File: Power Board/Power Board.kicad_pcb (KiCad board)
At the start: 2 copper layers, 80 x 45.7 mm, 61 parts, among them J1 Conn_02x15_Counter_Clockwise, Q1 SI7135DP, Q2 SI7135DP, Q3 SI7135DP, Q4 SI7135DP, Q5 SI7135DP, Q6 SI7135DP, U1 LTC4417CGN, U2 TPS54308DDC, U3 TPS54308DDC, U4 LTC3130-1

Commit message: Last commit before I change the board shape
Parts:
- moved C23 2.06 mm to (93.3, 116.2), turned to 270 degrees
- moved C20 1.27 mm to (96.0, 112.3)
- moved C22 1.27 mm to (95.5, 114.3)
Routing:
- net +3V3: track 79.0 -> 88.8 mm, vias 5 -> 9
- net /VCC_IN: track 114.2 -> 113.0 mm
- net Net-(C23-Pad1): track 2.15 -> 3.14 mm
- net GND: vias 87 -> 85
- removed copper zone on F.Cu, net +14V
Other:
- board text added: "Power Board v0.6 UAH SHC Spaceport America Cup 2018 Designed by Thomas Bennett & Daniel Corey"
- board text removed: "Power Board v0.5 UAH SHC Spaceport America Cup 2018 Designed by Thomas Bennett"

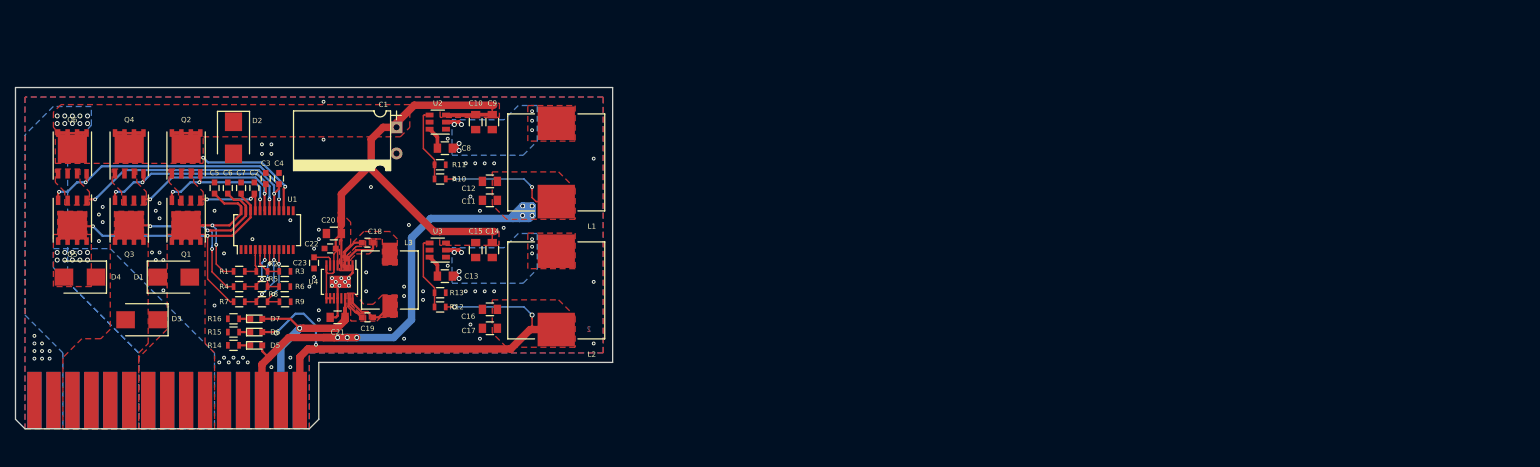
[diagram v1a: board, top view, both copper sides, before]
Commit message: New Board shape
Thanks a lot James
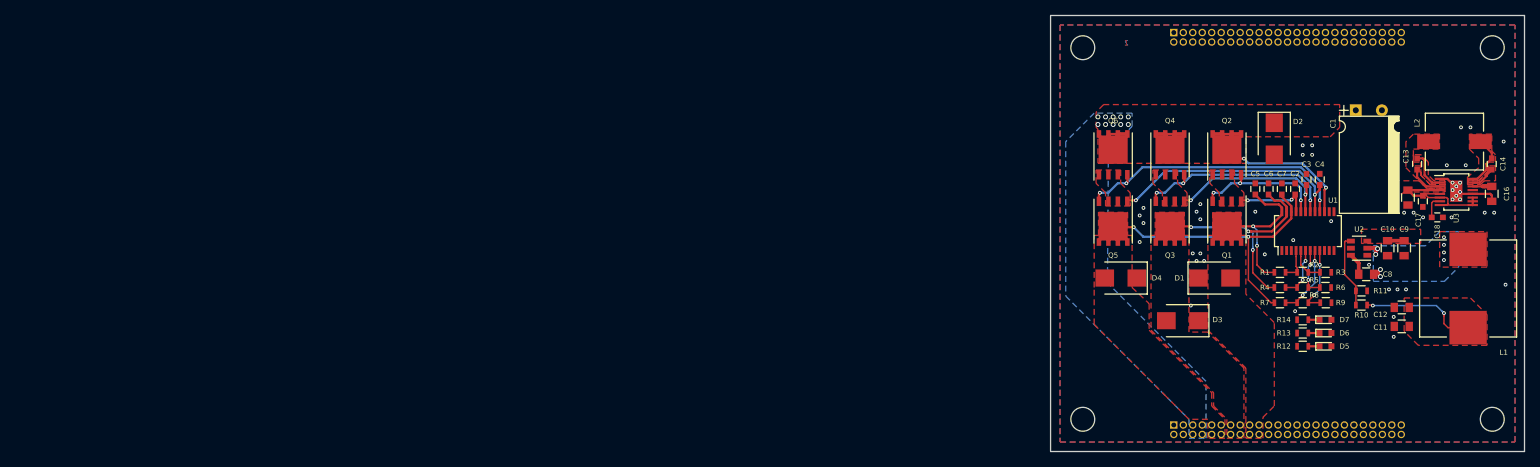
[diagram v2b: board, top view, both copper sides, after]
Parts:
- removed C19: 22nF, Capacitors_SMD:C_0603
- removed C20: 15 uF, Capacitors_SMD:C_0805
- removed C21: 22 uF, Capacitors_SMD:C_0805
- removed C22: 1 uF, Capacitors_SMD:C_0603
- removed C23: 4.7 uF, Capacitors_SMD:C_0603
- removed G***: LOGO, Custom Parts:Logo_v2
- removed L3: 15 uH, Custom Footprints:L_Wuerth_7447779115
- removed R15: 100 Ω, Resistors_SMD:R_0603
- removed R16: 470 Ω, Resistors_SMD:R_0603
- removed U4: LTC3130-1, Housings_SSOP:MSOP-16-1EP_3x4mm_Pitch0.5mm
- added H1: M3 Mounting Hole, Mounting_Holes:MountingHole_3.2mm_M3, F.Cu at (196.3, 87.4)
- added H2: M3 Mounting Hole, Mounting_Holes:MountingHole_3.2mm_M3, F.Cu at (251.2, 87.4)
- added H3: M3 Mounting Hole, Mounting_Holes:MountingHole_3.2mm_M3, F.Cu at (196.3, 137.2)
- added H4: M3 Mounting Hole, Mounting_Holes:MountingHole_3.2mm_M3, F.Cu at (251.2, 137.2)
- added J2: Conn_02x25_Odd_Even, Pin_Headers:Pin_Header_Straight_2x25_Pitch1.27mm, B.Cu at (208.5, 85.3)
- added SYM1: SYM_Arrow45_XLarge, Custom Parts:Logo_v3, B.Cu at (218.2, 121.9)
- C13: value 0.1 uF -> 22nF; footprint Capacitors_SMD:C_0805 -> Capacitors_SMD:C_0603
- C14: value 15 uF -> 22nF; footprint Capacitors_SMD:C_0805 -> Capacitors_SMD:C_0603
- C17: value 22 uF -> 1 uF; footprint Capacitors_SMD:C_0805 -> Capacitors_SMD:C_0603
- C18: value 22nF -> 4.7 uF
- J1: value Conn_02x15_Counter_Clockwise -> Conn_02x25_Odd_Even; footprint Custom Footprints:CONN_CARD_02x15_MALE -> Pin_Headers:Pin_Header_Straight_2x25_Pitch1.27mm; moved to B.Cu
- L2: value 18 uH -> 15 uH; footprint Inductors_SMD:L_Wuerth_HCI-1365 -> Custom Footprints:L_Wuerth_7447779115
- R12: value 100 kΩ -> 100 Ω
- R13: value 22 kΩ -> 100 Ω
- R14: value 100 Ω -> 470 Ω
- U3: value TPS54308DDC -> LTC3130-1; footprint TO_SOT_Packages_SMD:SOT-23-6 -> Housings_SSOP:MSOP-16-1EP_3x4mm_Pitch0.5mm
- moved C18 143.4 mm to (243.8, 110.1), turned to 0 degrees
- moved R14 143.3 mm to (225.8, 123.8)
- moved D5 143.3 mm to (228.9, 127.4)
- moved D6 143.3 mm to (228.9, 125.6)
- moved D7 143.3 mm to (228.9, 123.8)
- moved J1 141.2 mm to (208.5, 137.9), turned to 270 degrees
- moved C4 139.4 mm to (228.1, 105.0)
- moved C6 139.4 mm to (221.2, 106.3)
- moved D2 139.4 mm to (222.0, 99.6)
- moved D3 139.4 mm to (209.7, 124.0)
- moved D4 139.4 mm to (201.4, 118.2)
- moved Q3 139.4 mm to (208.0, 110.6)
- moved Q4 139.4 mm to (208.0, 101.7)
- moved R1 139.4 mm to (222.8, 117.5)
- moved R2 139.4 mm to (225.8, 117.5)
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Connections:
- C14 pad 1: /VCC_IN -> Net-(C14-Pad1)
- C14 pad 2: GND -> Net-(C14-Pad2)
- C16 pad 1: /XBEE_VCC -> +12V
- C17 pad 1: /XBEE_VCC -> /VCC_IN
- C18 pad 2: Net-(C18-Pad2) -> GND
- D6 pad 2: /XBEE_VCC -> +3V3
- J1 pad 10: /UMB_VCC -> /BAT_BAK_VCC
- J1 pad 11: GND -> /BAT_BAK_VCC
- J1 pad 12: GND -> /BAT_BAK_VCC
- J1 pad 13: +3V3 -> /BAT_VCC
- J1 pad 14: GND -> /BAT_VCC
- J1 pad 15: /XBEE_VCC -> /BAT_VCC
- J1 pad 16: GND -> /BAT_VCC
- J1 pad 17: +12V -> /UMB_VCC
- J1 pad 18: GND -> /UMB_VCC
- J1 pad 19: GND -> /UMB_VCC
- J1 pad 20: GND -> /UMB_VCC
- J1 pad 21: /BAT_BAK_VCC -> GND
- J1 pad 22: /BAT_BAK_VCC -> GND
- J1 pad 23: /BAT_BAK_VCC -> GND
- J1 pad 24: /BAT_BAK_VCC -> GND
- J1 pad 25: /VCC_IN -> (no net)
- J1 pad 26: /VCC_IN -> (no net)
- J1 pad 27: /VCC_IN -> (no net)
- J1 pad 28: /VCC_IN -> (no net)
- J1 pad 29: GND -> (no net)
- J1 pad 3: /BAT_VCC -> GND
- J1 pad 30: GND -> (no net)
- J1 pad 4: /BAT_VCC -> GND
- J1 pad 5: /BAT_VCC -> /VCC_IN
- J1 pad 6: /BAT_VCC -> /VCC_IN
- J1 pad 7: /UMB_VCC -> /VCC_IN
- J1 pad 8: /UMB_VCC -> /VCC_IN
- J1 pad 9: /UMB_VCC -> /BAT_BAK_VCC
- L2 pad 2: /XBEE_VCC -> Net-(C14-Pad1)
- R12 pad 1: /XBEE_VCC -> Net-(D5-Pad1)
- R12 pad 2: Net-(R12-Pad2) -> GND
- R13 pad 1: Net-(R12-Pad2) -> Net-(D6-Pad1)
- R14 pad 1: Net-(D5-Pad1) -> Net-(D7-Pad1)
- U3 pad 2: Net-(C13-Pad2) -> Net-(C13-Pad1)
- U3 pad 3: /VCC_IN -> Net-(C13-Pad2)
- U3 pad 4: Net-(R12-Pad2) -> /VCC_IN
- U3 pad 5: (no net) -> /VCC_IN
- U3 pad 6: Net-(C13-Pad1) -> /VCC_IN
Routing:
- net +3V3: track 88.8 -> 15.7 mm, vias 9 -> 2
- net /XBEE_VCC: track 70.9 -> 0.00 mm, vias 4 -> 0
- net /VCC_IN: track 113.0 -> 51.1 mm
- net +12V: track 26.9 -> 3.74 mm, vias 1 -> 0
- net Net-(R12-Pad2): track 9.96 -> 0.00 mm
- net Net-(C19-Pad1): track 7.04 -> 0.00 mm
- net Net-(C14-Pad1): track 0.00 -> 7.04 mm
- net Net-(C18-Pad2): track 4.58 -> 0.00 mm
- net Net-(C19-Pad2): track 3.36 -> 0.00 mm
- net Net-(C14-Pad2): track 0.00 -> 3.36 mm
- net Net-(C23-Pad1): track 3.14 -> 0.00 mm
- net Net-(C13-Pad1): track 2.98 -> 5.57 mm
- net Net-(C18-Pad1): track 5.57 -> 3.14 mm
- net Net-(C13-Pad2): track 5.67 -> 4.58 mm, vias 7 -> 0
- net Net-(C8-Pad2): track 5.67 -> 5.50 mm, vias 7 -> 8
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- removed copper zone on B.Cu, net /BAT_BAK_VCC
- removed copper zone on F.Cu, net /XBEE_VCC
- removed copper zone on B.Cu, net Net-(C13-Pad2)
- removed copper zone on F.Cu, net Net-(C13-Pad2)
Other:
- board size 80 x 45.7 mm -> 63.5 x 58.4 mm
- board text added: "Power Board v0.7 UAH SHC Spaceport America Cup 2018 Designed by Thomas Bennett & Daniel Corey"
- board text removed: "Power Board v0.6 UAH SHC Spaceport America Cup 2018 Designed by Thomas Bennett & Daniel Corey"

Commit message: A whole lot of changes
Kinda forgot what they all were
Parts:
- removed D1, D3, D4: SMBJ26CA, Diodes_SMD:D_SMB
- removed the D6 at (228.9, 125.6)
- removed the R13 at (225.8, 125.6)
- added J3: Conn_01x02, Custom Footprints:High_Current_Wires, F.Cu at (251.7, 117.6)
- added J4: Conn_01x02, Custom Footprints:High_Current_Wires, F.Cu at (251.7, 106.9)
- added J5: Conn_01x02, Custom Footprints:High_Current_Wires, F.Cu at (251.7, 96.0)
- J1: value Conn_02x25_Odd_Even -> Conn_02x10_Odd_Even; footprint Pin_Headers:Pin_Header_Straight_2x25_Pitch1.27mm -> Pin_Headers:Pin_Header_Straight_2x10_Pitch1.27mm
- J2: value Conn_02x25_Odd_Even -> Conn_01x02; footprint Pin_Headers:Pin_Header_Straight_2x25_Pitch1.27mm -> Custom Footprints:High_Current_Wires; moved to F.Cu
- moved J2 61.1 mm to (251.7, 128.5), turned to 90 degrees
- moved R12 40.9 mm to (200.7, 95.1), turned to 90 degrees
- moved D5 40.6 mm to (200.7, 98.2), turned to 270 degrees
- moved D6 39.6 mm to (198.6, 98.2), turned to 270 degrees
- moved R13 39.5 mm to (198.6, 95.1), turned to 90 degrees
- moved C13 35.3 mm to (207.6, 91.8)
- moved C14 35.3 mm to (217.6, 91.8)
- moved C15 35.3 mm to (206.4, 96.3)
- moved C16 35.3 mm to (217.6, 95.8)
- moved C17 35.3 mm to (208.4, 96.8)
- moved C18 35.3 mm to (210.3, 98.9)
- moved L2 35.3 mm to (212.6, 88.8)
- moved U3 35.3 mm to (212.9, 95.5)
- moved Q6 33.2 mm to (209.7, 133.6), turned to 180 degrees
- moved D2 33.2 mm to (201.9, 126.0)
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- renumbered D7 to D6, R14 to R13
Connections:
- J1 pad 1: GND -> +3V3
- J1 pad 11: /BAT_BAK_VCC -> (no net)
- J1 pad 12: /BAT_BAK_VCC -> GND
- J1 pad 13: /BAT_VCC -> (no net)
- J1 pad 14: /BAT_VCC -> +3V3
- J1 pad 15: /BAT_VCC -> (no net)
- J1 pad 16: /BAT_VCC -> GND
- J1 pad 17: /UMB_VCC -> (no net)
- J1 pad 18: /UMB_VCC -> +12V
- J1 pad 19: /UMB_VCC -> (no net)
- J1 pad 20: /UMB_VCC -> GND
- J1 pad 3: GND -> (no net)
- J1 pad 4: GND -> /VCC_IN
- J1 pad 5: /VCC_IN -> (no net)
- J1 pad 6: /VCC_IN -> /UMB_VCC
- J1 pad 7: /VCC_IN -> (no net)
- J1 pad 8: /VCC_IN -> /BAT_VCC
- J1 pad 9: /BAT_BAK_VCC -> (no net)
- J2 pad 1: (no net) -> /VCC_IN
- J2 pad 2: (no net) -> GND
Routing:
- net +3V3: track 15.7 -> 80.1 mm, vias 2 -> 4
- net /VCC_IN: track 51.1 -> 106.1 mm, vias 12 -> 23
- net +12V: track 3.74 -> 37.9 mm, vias 0 -> 2
- net /BAT_BAK_VCC: track 41.5 -> 56.9 mm, vias 2 -> 3
- net /BAT_VCC: track 30.9 -> 46.2 mm, vias 3 -> 4
- net /UMB_VCC: track 30.5 -> 45.5 mm, vias 2 -> 3
- net Net-(D6-Pad1) (its old number): track 1.50 -> 0.00 mm
- net GND: vias 47 -> 86
- added copper zone on F.Cu, net Net-(C13-Pad1)
- added copper zone on F.Cu, net Net-(C13-Pad2)
- added copper zone on F.Cu, net Net-(C14-Pad1)
- added copper zone on F.Cu, net Net-(C14-Pad2)
- removed copper zone on F.Cu, net Net-(C18-Pad1)
- removed copper zone on F.Cu, net Net-(C18-Pad2)
- removed copper zone on F.Cu, net Net-(C19-Pad1)
- removed copper zone on F.Cu, net Net-(C19-Pad2)
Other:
- board size 63.5 x 58.4 mm -> 55.9 x 58.4 mm
- board text added: "Backup Battery"
- board text added: "Main Battery"
- board text added: "Power Board v0.8 UAH SHC Spaceport America Cup 2018 Designed by Thomas Bennett Daniel Corey, Kyle Daigle, Jacob Klingbeil, Brendan Luke"
- board text added: "Servo Power"
- board text added: "Umbilical"
- board text removed: "Power Board v0.7 UAH SHC Spaceport America Cup 2018 Designed by Thomas Bennett & Daniel Corey"

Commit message: Added comments and stuff for power board PCB review
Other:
- board text added: "Connector for the other board underneath this one"
- board text added: "Having analog feedback lines for the power supply selector running right next to a high current trace is probably a bad idea but I'm hoping it'll be fine"
- board text added: "I hope running a trace under an inductor is okay"
- board text added: "Not sure about how thin this is"
- board text added: "Power Board v0.9 UAH SHC Spaceport America Cup 2018 Designed by Thomas Bennett Daniel Corey, Kyle Daigle, Jacob Klingbeil, Brendan Luke"
- board text added: "Super big traces with tons of vias since they have to handle 20 A"
- board text added: "The green lines are how much space I've been given in the rocket. The top part is a side view and the bottom part where the board is is a top-down view"
- board text added: "This is the DC-DC converter I used for CanSat, so I know for a fact it's not impossible to solder, even if you end up killing half the chips"
- board text added: "Wires will solder directly to these, and with XT60 (maybe XT30) connectors on the ends of the wires"
- board text removed: "Power Board v0.8 UAH SHC Spaceport America Cup 2018 Designed by Thomas Bennett Daniel Corey, Kyle Daigle, Jacob Klingbeil, Brendan Luke"
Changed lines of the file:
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@@
   (general
     (thickness 1.6)
-    (drawings 50)
+    (drawings 68)
     (tracks 493)
     (zones 0)
@@
     (39 F.Mask user)
     (40 Dwgs.User user)
-    (41 Cmts.User user hide)
+    (41 Cmts.User user)
     (42 Eco1.User user)
     (43 Eco2.User user hide)
@@
       (drillshape 0)
       (scaleselection 1)
-      (outputdirectory Gerbers/v0.8/))
+      (outputdirectory Gerbers/v0.9/))
   )
   (net 0 "")
@@
     )
   )
+  (gr_text "Connector for the other board underneath this one" (at 199.644 112.522 90) (layer Cmts.User)
+    (effects (font (size 0.5 0.5) (thickness 0.125)))
+  )
+  (gr_text "This is the DC-DC converter I used for CanSat,\nso I know for a fact it's not impossible to solder,\neven if you end up killing half the chips" (at 213.106 95.504) (layer Cmts.User)
+    (effects (font (size 0.5 0.5) (thickness 0.125)))
+  )
+  (gr_text "The green lines are how much space I've been given in the rocket. The top part is a side view and the bottom part where the board is is a top-down view" (at 224.282 74.168) (layer Cmts.User)
+    (effects (font (size 0.5 0.5) (thickness 0.125)))
+  )
+  (gr_text "Wires will solder directly to these, and with XT60 (maybe XT30) connectors on the ends of the wires" (at 252.984 111.252 90) (layer Cmts.User)
+    (effects (font (size 0.5 0.5) (thickness 0.125)))
+  )
+  (gr_text "I hope running a trace under an inductor is okay" (at 212.852 85.852) (layer Cmts.User)
+    (effects (font (size 0.5 0.5) (thickness 0.125)))
+  )
+  (gr_line (start 226.06 114.554) (end 228.346 112.014) (layer Cmts.User) (width 0.2))
+  (gr_line (start 221.996 114.554) (end 226.06 114.554) (layer Cmts.User) (width 0.2))
+  (gr_line (start 221.996 116.586) (end 221.996 114.554) (layer Cmts.User) (width 0.2))
+  (gr_line (start 226.314 116.586) (end 221.996 116.586) (layer Cmts.User) (width 0.2))
+  (gr_line (start 230.632 112.014) (end 226.314 116.586) (layer Cmts.User) (width 0.2))
+  (gr_line (start 228.346 112.014) (end 230.632 112.014) (layer Cmts.User) (width 0.2))
+  (gr_text "Having analog feedback lines for the power supply\nselector running right next to a high current trace\nis probably a bad idea but I'm hoping it'll be fine" (at 227.584 110.236) (layer Cmts.User)
+    (effects (font (size 0.5 0.5) (thickness 0.125)))
+  )
+  (gr_line (start 212.598 128.524) (end 212.598 123.444) (layer Cmts.User) (width 0.2))
+  (gr_line (start 215.392 128.524) (end 212.598 128.524) (layer Cmts.User) (width 0.2))
+  (gr_line (start 215.392 123.444) (end 215.392 128.524) (layer Cmts.User) (width 0.2))
+  (gr_line (start 212.598 123.444) (end 215.392 123.444) (layer Cmts.User) (width 0.2))
+  (gr_text "Not sure about how thin this is" (at 214.122 122.428) (layer Cmts.User)
+    (effects (font (size 0.5 0.5) (thickness 0.125)))
+  )
+  (gr_text "Super big traces with tons\nof vias since they have to\nhandle 20 A" (at 232.156 123.19) (layer Cmts.User)
+    (effects (font (size 0.5 0.5) (thickness 0.125)))
+  )
   (dimension 29.21 (width 0.125) (layer Dwgs.User)
     (gr_text "1.1500 in" (at 203.192 97.663 90) (layer Dwgs.User)
@@
   (gr_line (start 223.647 78.105) (end 293.243 78.105) (layer Eco1.User) (width 0.2))
   (gr_line (start 223.647 78.105) (end 154.051 78.105) (layer Eco1.User) (width 0.2))
-  (gr_text "Power Board v0.8\nUAH SHC Spaceport America Cup 2018\nDesigned by Thomas Bennett\nDaniel Corey, Kyle Daigle,\nJacob Klingbeil, Brendan Luke" (at 239.776 89.408) (layer B.SilkS)
+  (gr_text "Power Board v0.9\nUAH SHC Spaceport America Cup 2018\nDesigned by Thomas Bennett\nDaniel Corey, Kyle Daigle,\nJacob Klingbeil, Brendan Luke" (at 239.776 89.408) (layer B.SilkS)
     (effects (font (size 1 1) (thickness 0.15)) (justify left mirror))
   )

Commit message: Removed Voltage sensing from main board, added 2 PTs
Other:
- board text added: "I'm aware this is bad"
